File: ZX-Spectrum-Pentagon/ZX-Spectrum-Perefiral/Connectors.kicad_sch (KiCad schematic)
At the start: 2 parts

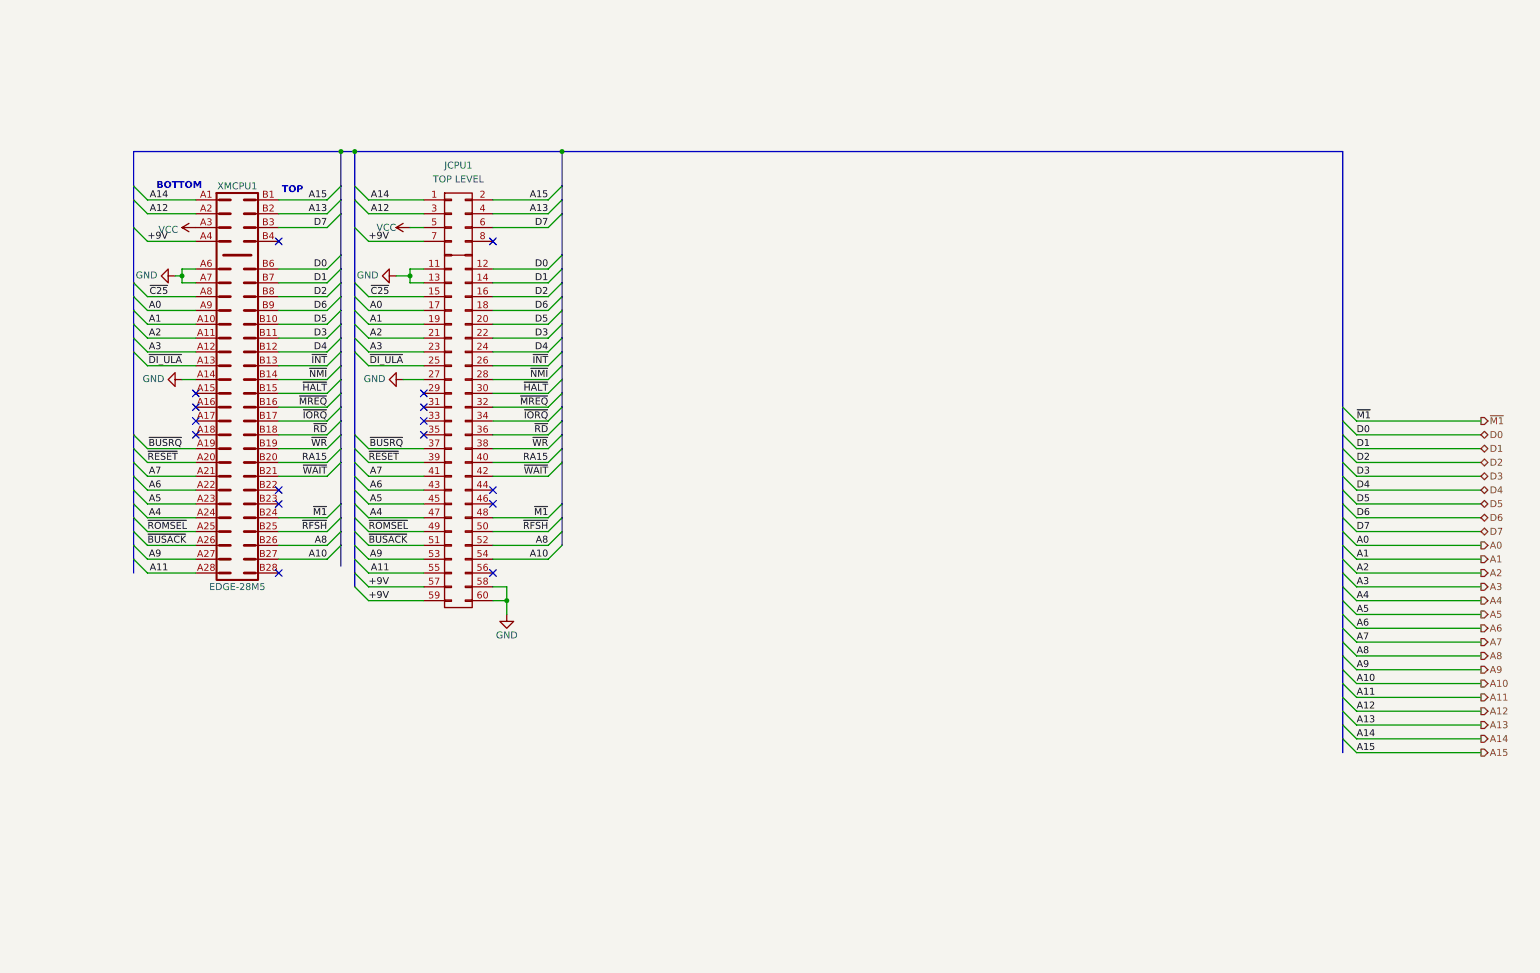
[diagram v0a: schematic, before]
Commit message: CPU.kicad_sch non functional changes update fdd controller
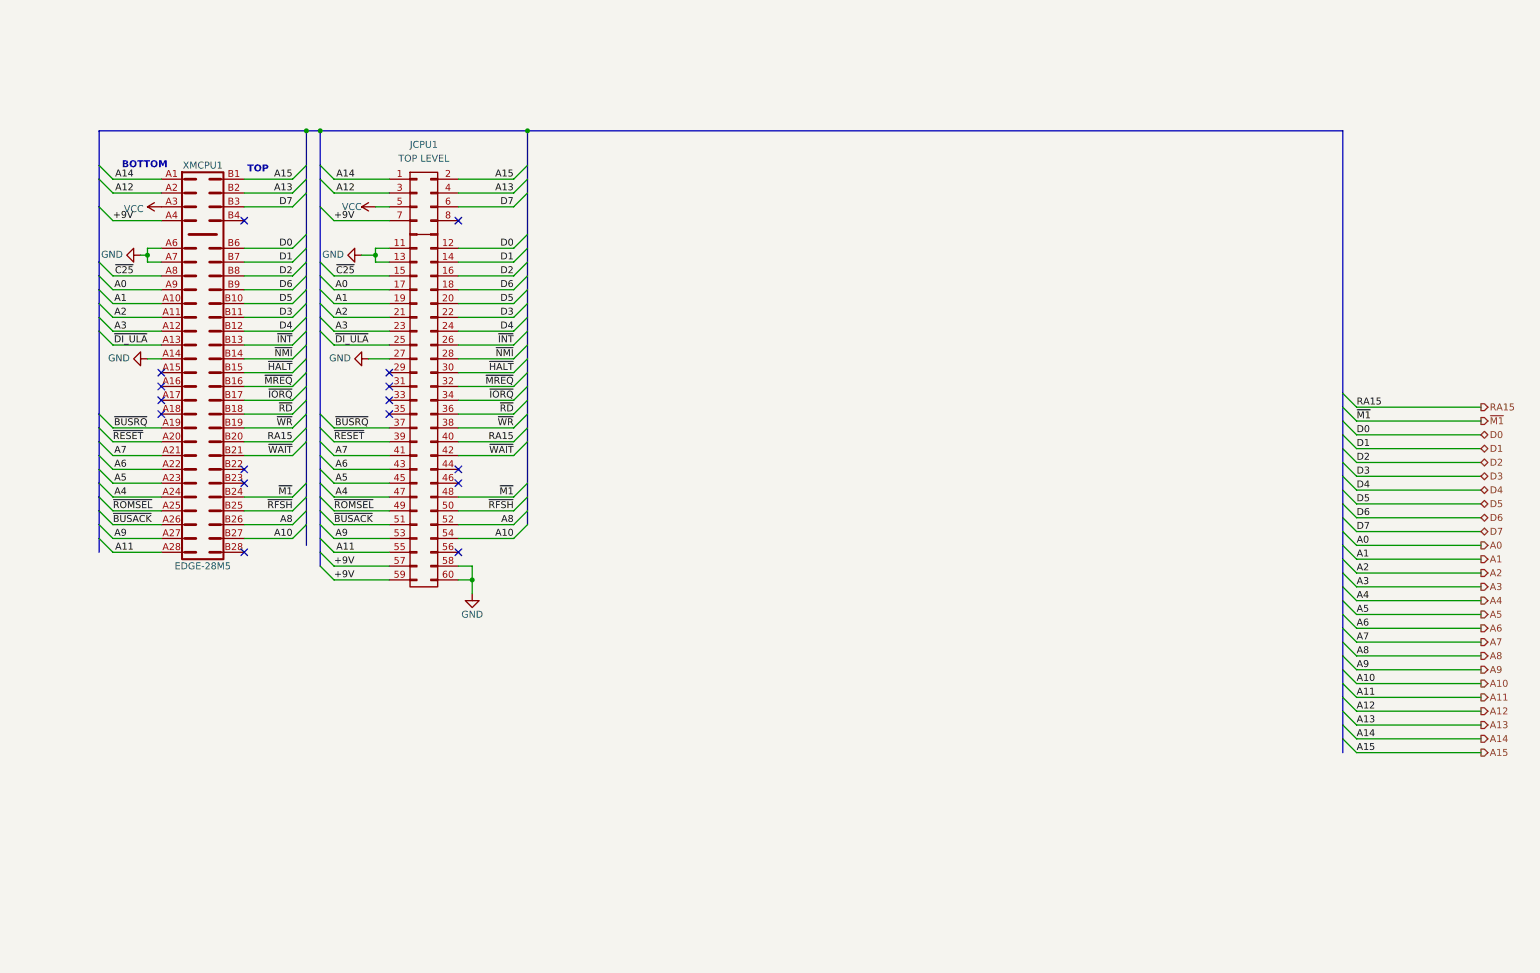
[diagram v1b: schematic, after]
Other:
- moved on the sheet: JCPU1, XMCPU1

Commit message: improve schematic fdc
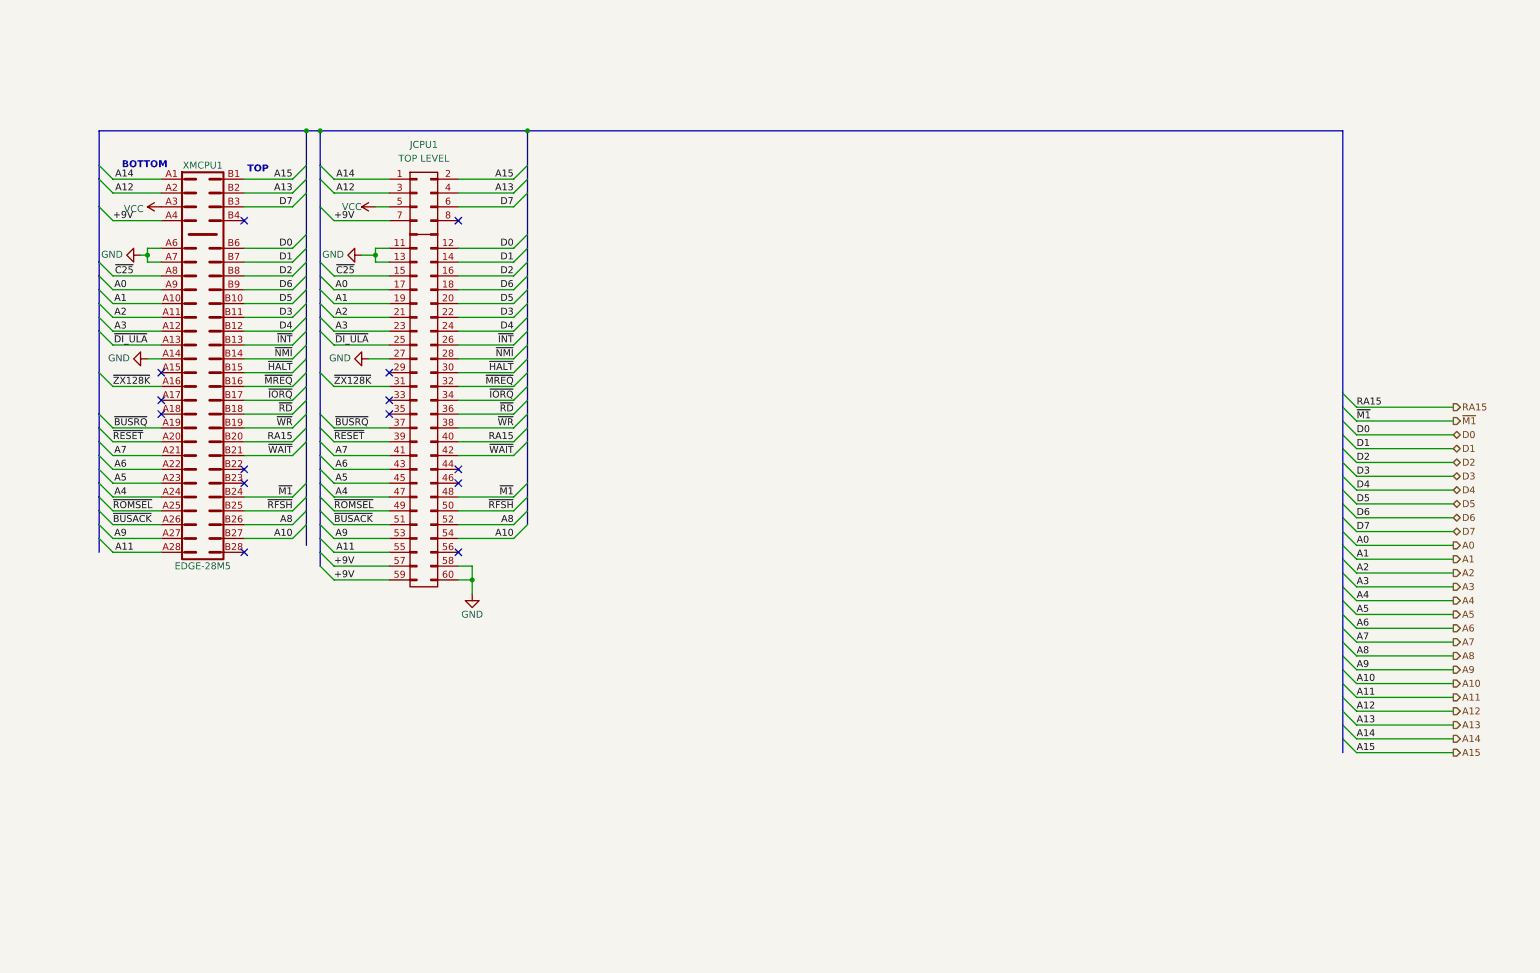
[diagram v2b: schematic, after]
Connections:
- net ~{ZX128K}: now reaches XMCPU1.A16
- net ~{ZX128K}: now also JCPU1.31 (Pin_31)
- no-connect marks 16 -> 14

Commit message: add keywords for some symbol in library 74IEC update some symbol in zx_custom_symbol improve FDC, Connectors, ZX-Spectrum-Perefiral schematic
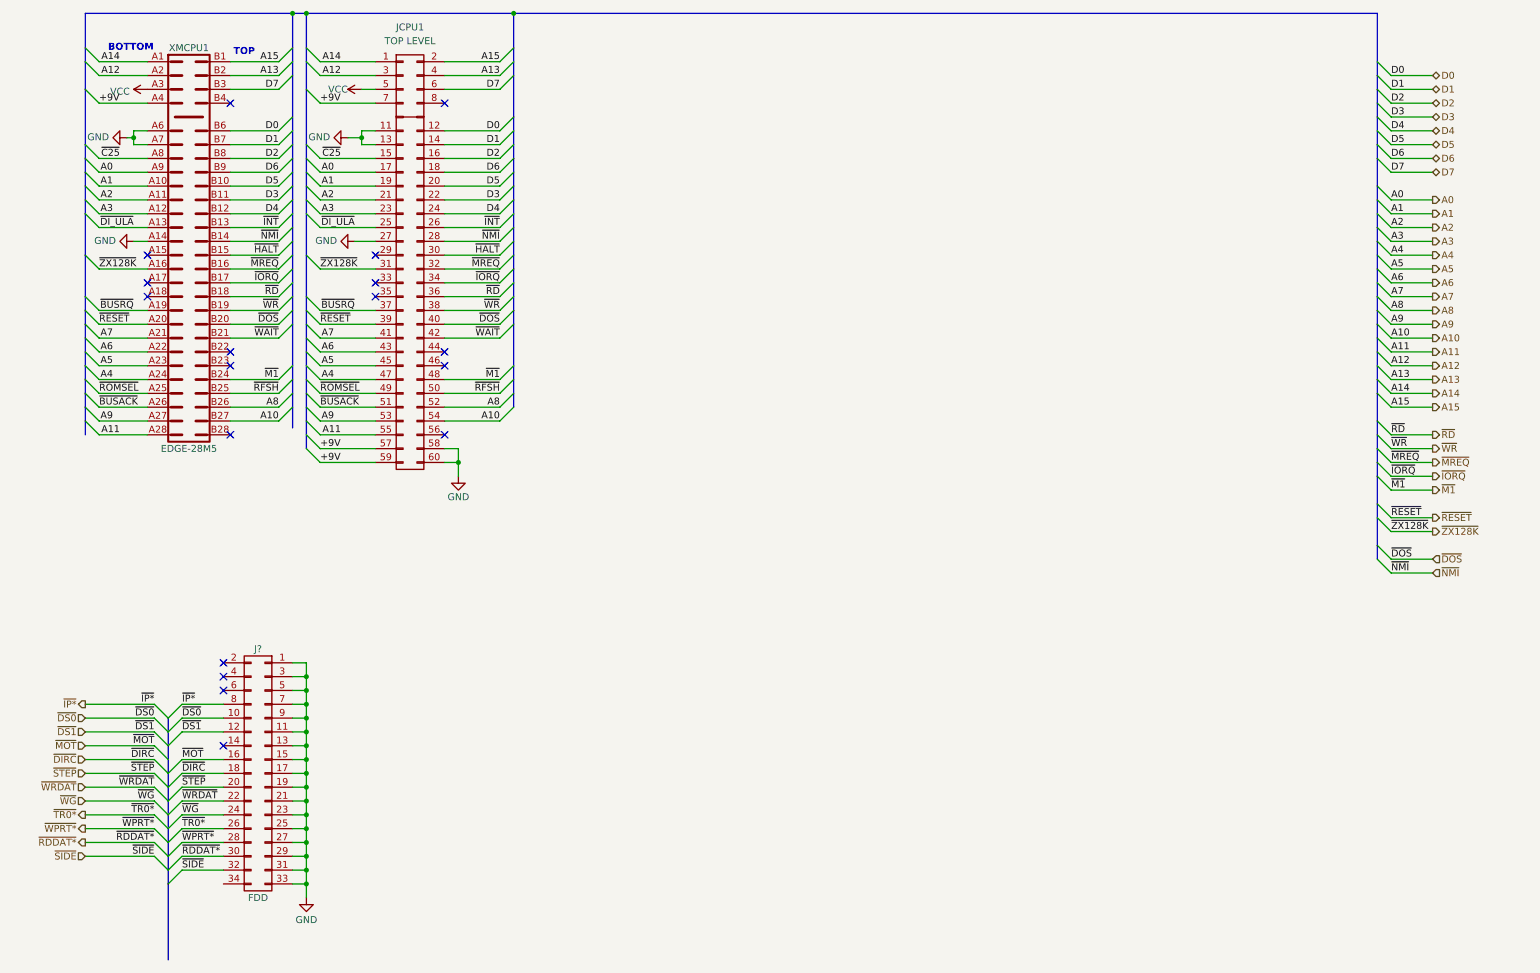
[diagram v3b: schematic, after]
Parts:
- added J?: FDD, Connector_IDC:IDC-Header_2x17_P2.54mm_Vertical, symbol zx_custom_symbol:Conn_02x17_Odd_Even
- XMCPU1: footprint ZX-Spectrum-Pentagon:EDGE_28M5-2.54 -> edge:EDGE_3M_0-2.54
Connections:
- net GND: now also J?.1 (Pin_1), J?.11 (Pin_11), J?.13 (Pin_13), J?.15 (Pin_15), J?.17 (Pin_17), J?.19 (Pin_19), J?.21 (Pin_21), J?.23 (Pin_23), J?.25 (Pin_25), J?.27 (Pin_27), J?.29 (Pin_29), J?.3 (Pin_3), J?.31 (Pin_31), J?.33 (Pin_33), J?.5 (Pin_5), J?.7 (Pin_7), J?.9 (Pin_9)
- net RA15 renamed ~{DOS}
- new net ~{DIRC}: J?.18 (Pin_18)
- new net ~{DS0}: J?.10 (Pin_10)
- new net ~{DS1}: J?.12 (Pin_12)
- new net ~{IP*}: J?.8 (Pin_8)
- new net ~{MOT}: J?.16 (Pin_16)
- new net ~{RDDAT*}: J?.30 (Pin_30)
- new net ~{SIDE}: J?.32 (Pin_32)
- new net ~{STEP}: J?.20 (Pin_20)
- new net ~{TR0*}: J?.26 (Pin_26)
- new net ~{WG}: J?.24 (Pin_24)
- new net ~{WPRT*}: J?.28 (Pin_28)
- new net ~{WRDAT}: J?.22 (Pin_22)
- no-connect marks 14 -> 18
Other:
- title: (none) -> ZX-Pentagon-Pereferal
- moved on the sheet: JCPU1, XMCPU1

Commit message: update ZX-Spectrum-Perefiral
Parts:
- added J1: IDE, Connector_IDC:IDC-Header_2x20_P2.54mm_Vertical, symbol zx_custom_symbol:Conn_02x20_Odd_Even
- gave numbers to parts that had none: 1
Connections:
- net GND: now also J1.19 (Pin_19), J1.2 (Pin_2), J1.22 (Pin_22), J1.24 (Pin_24), J1.26 (Pin_26), J1.30 (Pin_30), J1.40 (Pin_40)
- new net HA0: J1.35 (Pin_35)
- new net HA1: J1.33 (Pin_33)
- new net HA2: J1.36 (Pin_36)
- new net HD0: J1.17 (Pin_17)
- new net HD1: J1.15 (Pin_15)
- new net HD10: J1.8 (Pin_8)
- new net HD11: J1.10 (Pin_10)
- new net HD12: J1.12 (Pin_12)
- new net HD13: J1.14 (Pin_14)
- new net HD14: J1.16 (Pin_16)
- new net HD15: J1.18 (Pin_18)
- new net HD2: J1.13 (Pin_13)
- new net HD3: J1.11 (Pin_11)
- new net HD4: J1.9 (Pin_9)
- new net HD5: J1.7 (Pin_7)
- new net HD6: J1.5 (Pin_5)
- new net HD7: J1.3 (Pin_3)
- new net HD8: J1.4 (Pin_4)
- new net HD9: J1.6 (Pin_6)
- new net ~{ACT}: J1.39 (Pin_39)
- new net ~{HCS0}: J1.37 (Pin_37)
- new net ~{HCS1}: J1.38 (Pin_38)
- new net ~{HIOR}: J1.25 (Pin_25)
- new net ~{HIOW}: J1.23 (Pin_23)
- new net ~{HRESET}: J1.1 (Pin_1)
- no-connect marks 18 -> 26

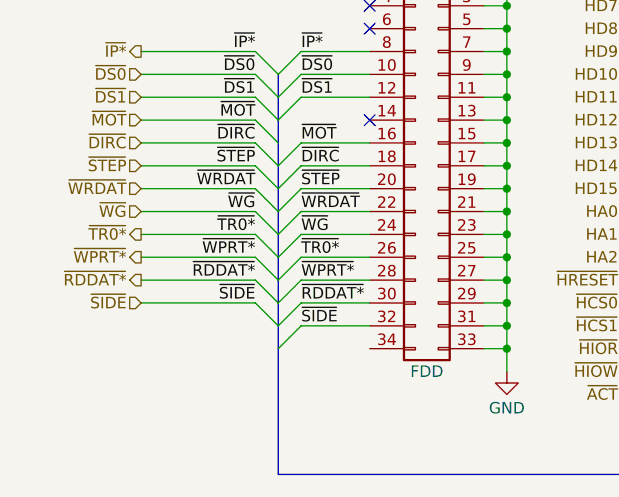
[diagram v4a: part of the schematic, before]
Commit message: fix 74ICE, FDControlers, edge_lib library update all schematic and board fix ERC ZX-Spectrum-Perefiral
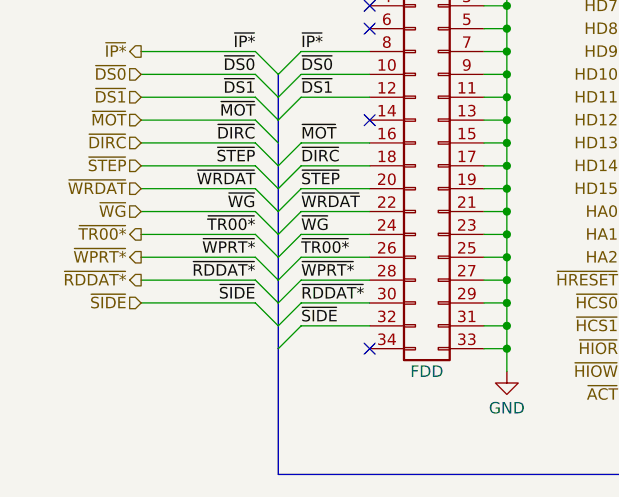
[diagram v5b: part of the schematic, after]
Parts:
- XMCPU1: footprint edge:EDGE_3M_0-2.54 -> edge:EDGE_28M5-2.54
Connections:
- net ~{TR0*} renamed ~{TR00*}
- no-connect marks 26 -> 27
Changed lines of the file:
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@@
 	)
 	(no_connect
+		(at 48.26 176.53)
+	)
+	(no_connect
 		(at 101.6 163.83)
 	)
@@
 	)
 	(bus_entry
+		(at 86.36 171.45)
+		(size 2.54 2.54)
+		(stroke
+			(width 0)
+			(type default)
+		)
+	)
+	(bus_entry
 		(at 91.44 176.53)
 		(size -2.54 2.54)
@@
 	)
 	(bus_entry
-		(at 86.36 171.45)
-		(size 2.54 2.54)
-		(stroke
-			(width 0)
-			(type default)
-		)
-	)
-	(bus_entry
 		(at 101.6 66.04)
 		(size -2.54 2.54)
@@
 	(wire
 		(pts
-			(xy 77.47 171.45) (xy 86.36 171.45)
-		)
-		(stroke
-			(width 0)
-			(type default)
-		)
-	)
-	(wire
-		(pts
 			(xy 49.53 30.48) (xy 58.42 30.48)
 		)
@@
 	(wire
 		(pts
+			(xy 77.47 171.45) (xy 86.36 171.45)
+		)
+		(stroke
+			(width 0)
+			(type default)
+		)
+	)
+	(wire
+		(pts
 			(xy 262.89 88.9) (xy 270.51 88.9)
 		)
@@
 		)
 	)
-	(label "~{TR0*}"
+	(label "~{TR00*}"
 		(at 40.64 166.37 0)
 		(fields_autoplaced yes)
@@
 		)
 	)
-	(label "~{TR0*}"
+	(label "~{TR00*}"
 		(at 35.56 163.83 180)
 		(fields_autoplaced yes)
@@
 		)
 	)
-	(hierarchical_label "~{TR0*}"
+	(hierarchical_label "~{TR00*}"
 		(shape output)
 		(at 22.86 163.83 180)
@@
 			)
 		)
-		(property "Footprint" "edge:EDGE_3M_0-2.54"
+		(property "Footprint" "edge:EDGE_28M5-2.54"
 			(at 41.91 20.32 0)
 			(effects
